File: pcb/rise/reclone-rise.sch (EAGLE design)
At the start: 133 parts, among them Y1 12MHz, Y4 32K768

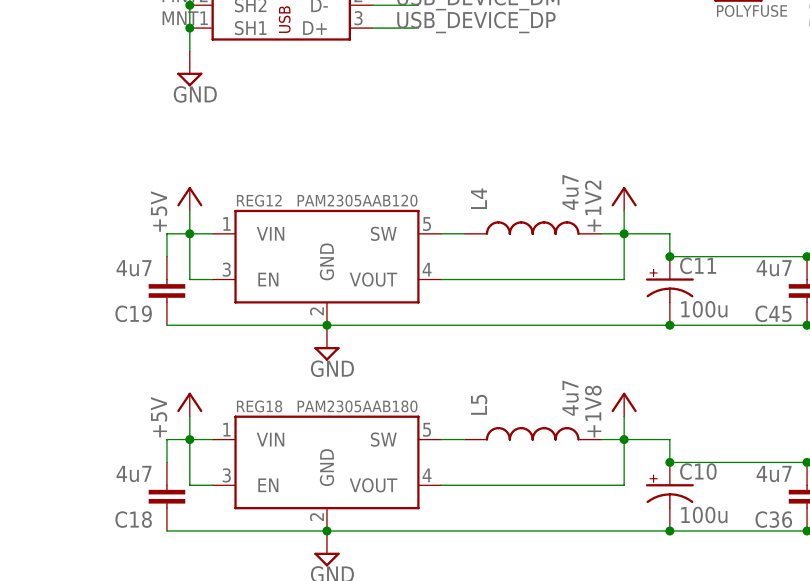
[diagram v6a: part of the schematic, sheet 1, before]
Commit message: Populated several more parts and replaced 1.8V regulator with one that's in stock at Digikey
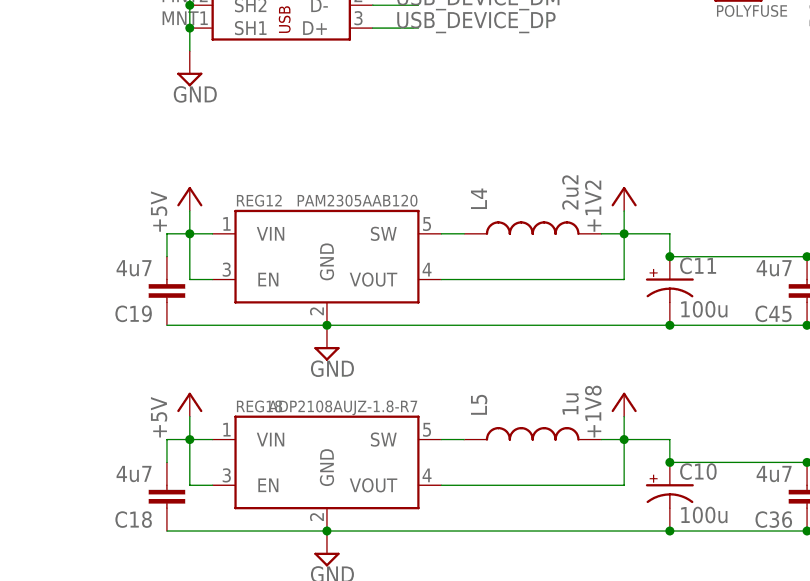
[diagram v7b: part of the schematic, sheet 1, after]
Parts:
- BAT: DIGIKEY# (none) -> BK-885-ND; MANF (none) -> MPD (Memory Protection Devices); MANF# (none) -> BK-885
- BOOT, BUSPWR: DIGIKEY# (none) -> 952-1770-ND; MANF (none) -> Harwin Inc.; MANF# (none) -> M20-9770246
- F1: DIGIKEY# (none) -> MF-NSMF150-2CT-ND; MANF (none) -> Bourns Inc.; MANF# (none) -> MF-NSMF150-2
- FPGA: DIGIKEY# (none) -> 122-1672-ND; MANF (none) -> Xilinx Inc.; MANF# (none) -> XC6SLX16-2FTG256C
- L4: value 4u7 -> 2u2
- L5: value 4u7 -> 1u
- REG12: DIGIKEY# (none) -> PAM2305AAB120DICT-ND; MANF (none) -> Diodes Incorporated; MANF# (none) -> PAM2305AAB120
- REG18: value PAM2305AAB180 -> ADP2108AUJZ-1.8-R7; DIGIKEY# (none) -> ADP2108AUJZ-1.8-R7CT-ND; MANF (none) -> Analog Devices Inc.; MANF# (none) -> ADP2108AUJZ-1.8-R7
- REG33: DIGIKEY# (none) -> PAM2305AAB330DICT-ND; MANF (none) -> Diodes Incorporated; MANF# (none) -> PAM2305AAB330
- RGB: DIGIKEY# (none) -> 365-1410-1-ND; MANF (none) -> TT Electronics/Optek Technology; MANF# (none) -> OVSRRGBCC3
- USER: DIGIKEY# (none) -> EG1840-ND; MANF (none) -> E-Switch; MANF# (none) -> TL1105SF250Q

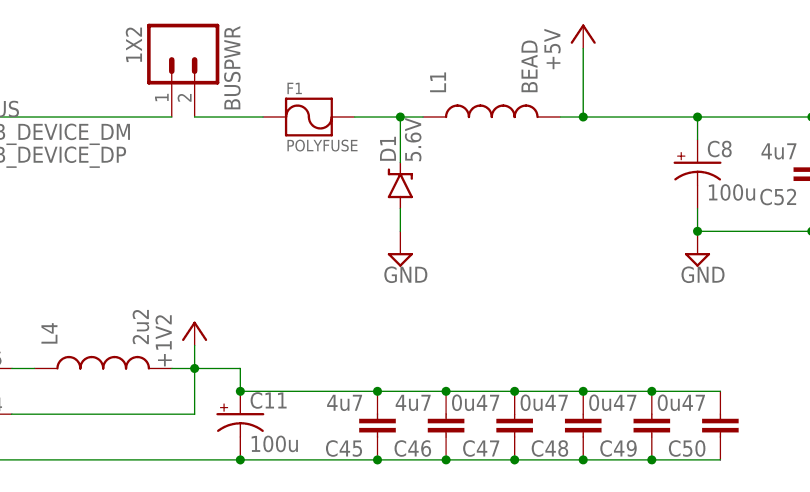
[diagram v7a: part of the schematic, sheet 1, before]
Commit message: Populated some BOM info
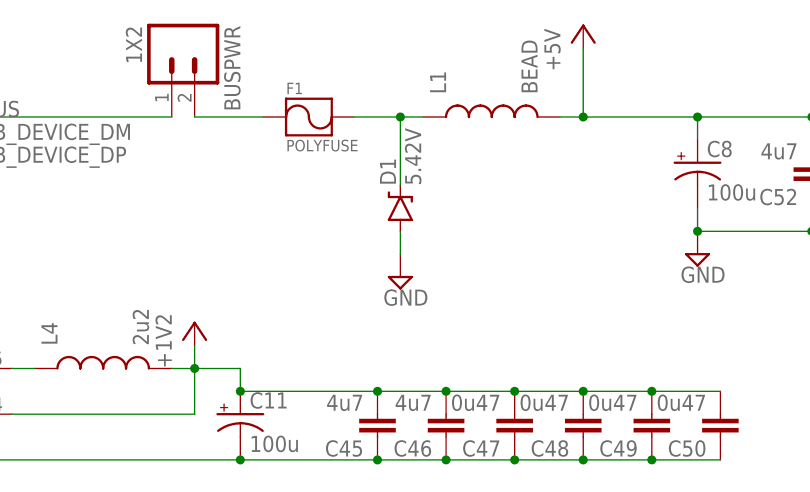
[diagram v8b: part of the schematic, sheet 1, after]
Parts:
- ACT: DIGIKEY# (none) -> 732-4978-1-ND; MANF (none) -> Wurth Electronics Inc.; MANF# (none) -> 150060RS75000
- D1: value 5.6V -> 5.42V; DIGIKEY# (none) -> DDZ5V6ASF-7DICT-ND; MANF (none) -> Diodes Incorporated; MANF# (none) -> DDZ5V6ASF-7
- USB: DIGIKEY# (none) -> AE11131-ND; MANF (none) -> Assmann WSW Components; MANF# (none) -> AU-Y1008-2
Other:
- moved on the sheet: D1
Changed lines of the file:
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@@
 </classes>
 <parts>
-<part name="USB" library="reclone-rise" deviceset="USB_A_2H" device=""/>
+<part name="USB" library="reclone-rise" deviceset="USB_A_2H" device="">
+<attribute name="DIGIKEY#" value="AE11131-ND"/>
+<attribute name="MANF" value="Assmann WSW Components"/>
+<attribute name="MANF#" value="AU-Y1008-2"/>
+</part>
 <part name="DVI" library="reclone-rise" deviceset="TMDS_A" device="">
 <attribute name="DIGIKEY#" value="609-4614-1-ND"/>
@@
 <part name="SUPPLY27" library="supply2" deviceset="GND" device=""/>
 <part name="P+7" library="supply1" deviceset="+5V" device=""/>
-<part name="ACT" library="SparkFun-LED" deviceset="LED" device="0603" value="RED"/>
+<part name="ACT" library="SparkFun-LED" deviceset="LED" device="0603" value="RED">
+<attribute name="DIGIKEY#" value="732-4978-1-ND"/>
+<attribute name="MANF" value="Wurth Electronics Inc."/>
+<attribute name="MANF#" value="150060RS75000"/>
+</part>
 <part name="R9" library="SparkFun-Passives" deviceset="RESISTOR" device="0603-RES" value="160"/>
 <part name="SUPPLY30" library="supply2" deviceset="GND" device=""/>
@@
 <part name="L2" library="SparkFun-Passives" deviceset="INDUCTOR" device="0603" value="BEAD"/>
 <part name="L3" library="SparkFun-Passives" deviceset="INDUCTOR" device="0603" value="BEAD"/>
-<part name="D1" library="SparkFun-DiscreteSemi" deviceset="DIODE-ZENER" device="5.6V" value="5.6V"/>
+<part name="D1" library="SparkFun-DiscreteSemi" deviceset="DIODE-ZENER" device="5.6V" value="5.42V">
+<attribute name="DIGIKEY#" value="DDZ5V6ASF-7DICT-ND"/>
+<attribute name="MANF" value="Diodes Incorporated"/>
+<attribute name="MANF#" value="DDZ5V6ASF-7"/>
+</part>
 <part name="SUPPLY32" library="supply2" deviceset="GND" device=""/>
 <part name="SUPPLY33" library="supply2" deviceset="GND" device=""/>
@@
 </plain>
 <instances>
-<instance part="USB" gate="USB_A_2H" x="353.06" y="121.92"/>
+<instance part="USB" gate="USB_A_2H" x="353.06" y="121.92">
+<attribute name="DIGIKEY#" x="353.06" y="121.92" size="1.778" layer="96" display="off"/>
+<attribute name="MANF" x="353.06" y="121.92" size="1.778" layer="96" display="off"/>
+<attribute name="MANF#" x="353.06" y="121.92" size="1.778" layer="96" display="off"/>
+</instance>
 <instance part="DEBUG" gate="G$1" x="43.18" y="238.76" rot="R180">
 <attribute name="DIGIKEY#" x="43.18" y="238.76" size="1.778" layer="96" rot="R180" display="off"/>
@@
 <instance part="SUPPLY27" gate="GND" x="213.36" y="213.36"/>
 <instance part="P+7" gate="1" x="116.84" y="246.38"/>
-<instance part="ACT" gate="G$1" x="233.68" y="96.52" rot="R90"/>
+<instance part="ACT" gate="G$1" x="233.68" y="96.52" rot="R90">
+<attribute name="DIGIKEY#" x="233.68" y="96.52" size="1.778" layer="96" rot="R90" display="off"/>
+<attribute name="MANF" x="233.68" y="96.52" size="1.778" layer="96" rot="R90" display="off"/>
+<attribute name="MANF#" x="233.68" y="96.52" size="1.778" layer="96" rot="R90" display="off"/>
+</instance>
 <instance part="R9" gate="G$1" x="223.52" y="96.52" smashed="yes">
 <attribute name="NAME" x="217.932" y="96.7486" size="1.778" layer="95"/>
@@
 <instance part="L2" gate="G$1" x="30.48" y="121.92" rot="R90"/>
 <instance part="L3" gate="G$1" x="38.1" y="129.54" rot="R90"/>
-<instance part="D1" gate="G$1" x="96.52" y="228.6" rot="R90"/>
-<instance part="SUPPLY32" gate="GND" x="96.52" y="220.98"/>
+<instance part="D1" gate="G$1" x="96.52" y="226.06" rot="R90">
+<attribute name="DIGIKEY#" x="96.52" y="226.06" size="1.778" layer="96" rot="R90" display="off"/>
+<attribute name="MANF" x="96.52" y="226.06" size="1.778" layer="96" rot="R90" display="off"/>
+<attribute name="MANF#" x="96.52" y="226.06" size="1.778" layer="96" rot="R90" display="off"/>
+</instance>
+<instance part="SUPPLY32" gate="GND" x="96.52" y="218.44"/>
 <instance part="REG12" gate="VREG" x="40.64" y="205.74">
 <attribute name="DIGIKEY#" x="40.64" y="205.74" size="1.778" layer="96" display="off"/>
@@
 <pinref part="D1" gate="G$1" pin="A"/>
 <pinref part="SUPPLY32" gate="GND" pin="GND"/>
-<wire x1="96.52" y1="223.52" x2="96.52" y2="226.06" width="0.1524" layer="91"/>
+<wire x1="96.52" y1="220.98" x2="96.52" y2="223.52" width="0.1524" layer="91"/>
 </segment>
 <segment>
@@
 <pinref part="D1" gate="G$1" pin="C"/>
 <wire x1="96.52" y1="236.22" x2="91.44" y2="236.22" width="0.1524" layer="91"/>
-<wire x1="96.52" y1="231.14" x2="96.52" y2="236.22" width="0.1524" layer="91"/>
+<wire x1="96.52" y1="228.6" x2="96.52" y2="236.22" width="0.1524" layer="91"/>
 <junction x="96.52" y="236.22"/>
 </segment>
